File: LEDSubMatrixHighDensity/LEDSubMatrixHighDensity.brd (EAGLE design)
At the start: 16.9 x 135 mm, 129 parts, among them IC1 TLC5955DCAR, IC2 TLC5955DCAR, IC3 TLC5955DCAR, IC4 TLC5955DCAR, IC5 TLC5955DCAR, IC6 TLC5955DCAR, IC7 TLC5955DCAR, IC8 TLC5955DCAR

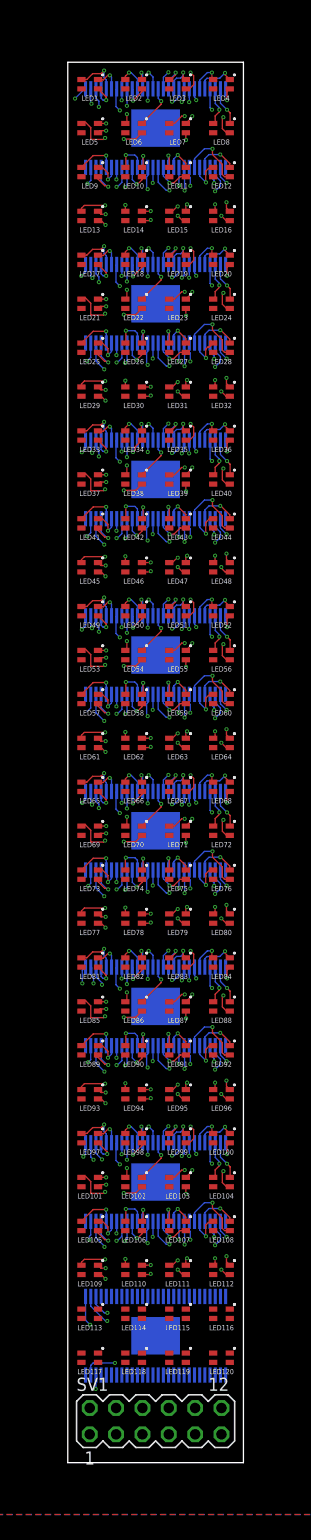
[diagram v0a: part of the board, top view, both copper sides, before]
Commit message: Finished routing traces on high density matrix PCB
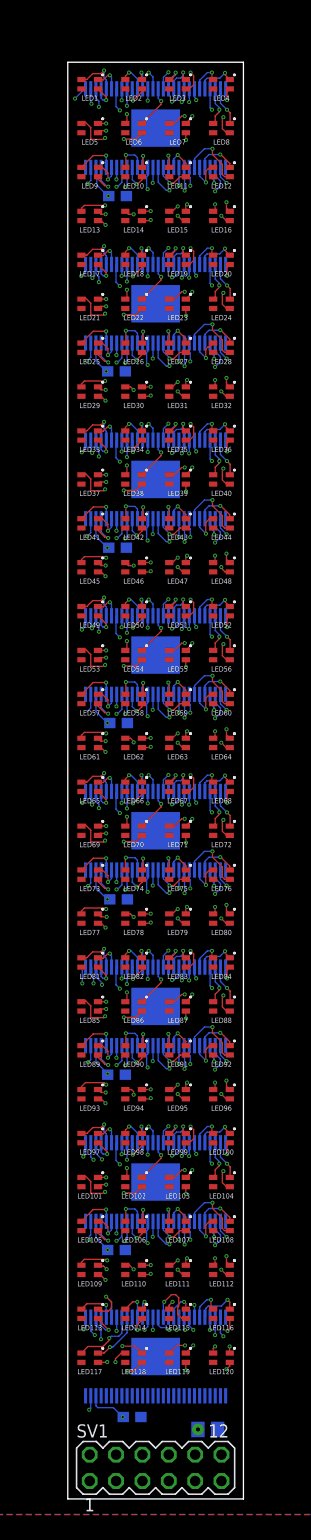
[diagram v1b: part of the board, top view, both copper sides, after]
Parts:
- added C1, C2, C3, C4, C5, C6, C7, C8: .1uF, rcl:C0603
- added C9: 10uF, rcl:C0805
- moved SV1 4.50 mm to (8.47, -135.5)
- moved IC8 2.00 mm to (8.47, -124.8)
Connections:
- net 3V3: now also C1.1, C2.1, C3.1, C4.1, C5.1, C6.1, C7.1, C8.1, C9.1
- net GND: now also C1.2, C2.2, C3.2, C4.2, C5.2, C6.2, C7.2, C8.2, C9.2
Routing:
- net N$LEDG118_IC8_PIN15: track 0.00 -> 11.0 mm, vias 0 -> 2
- net N$LEDR118_IC8_PIN14: track 0.00 -> 9.08 mm, vias 0 -> 2
- net 3V3: track 18.4 -> 26.6 mm, vias 7 -> 9
- net N$LEDB118_IC8_PIN13: track 0.00 -> 7.77 mm, vias 0 -> 2
- net N$LEDB120_IC8_PIN25: track 0.00 -> 7.18 mm, vias 0 -> 2
- net N$LEDB116_IC8_PIN22: track 0.00 -> 6.71 mm, vias 0 -> 2
- net N$LEDB119_IC8_PIN19: track 0.00 -> 6.59 mm, vias 0 -> 2
- net N$LEDR117_IC8_PIN8: track 0.00 -> 6.35 mm, vias 0 -> 1
- net N$LEDB115_IC8_PIN16: track 0.00 -> 5.92 mm, vias 0 -> 1
- net N$LEDB117_IC8_PIN7: track 0.00 -> 5.60 mm, vias 0 -> 2
- net N$LEDG117_IC8_PIN9: track 0.00 -> 5.11 mm, vias 0 -> 1
- net N$LEDG113_IC8_PIN6: track 0.00 -> 5.01 mm, vias 0 -> 1
- net LAT: track 144.8 -> 149.7 mm
- net SIN_5,6: track 63.0 -> 67.7 mm
- net N$LEDR119_IC8_PIN20: track 0.00 -> 4.58 mm, vias 0 -> 2
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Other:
- board size 16.9 x 135 mm -> 16.9 x 138.5 mm

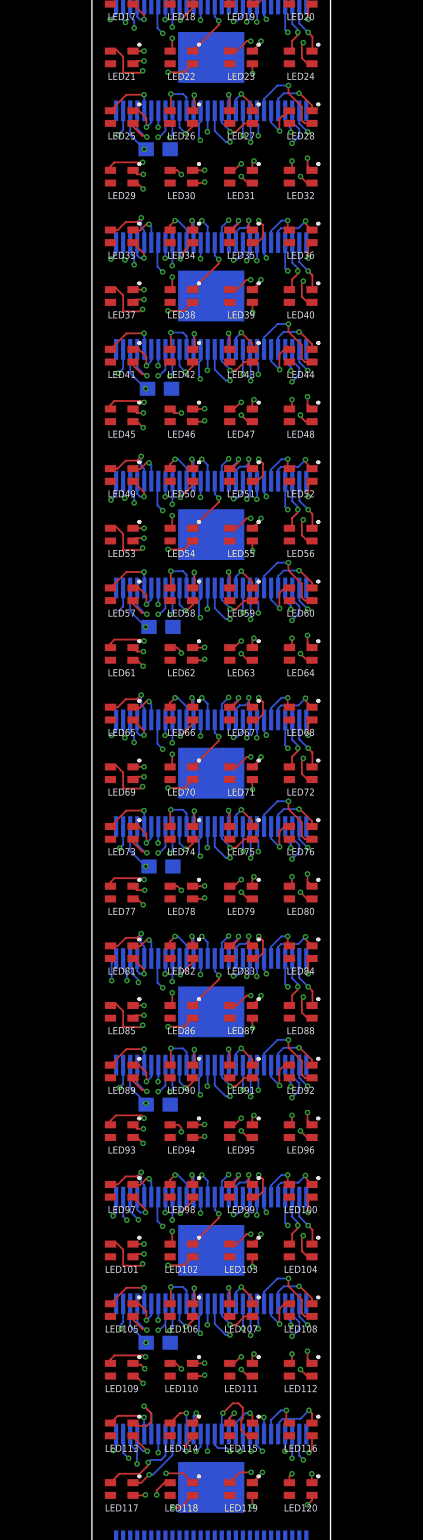
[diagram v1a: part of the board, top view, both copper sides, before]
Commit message: High density PCB fixes
Fixed airwires errors and grouped components on schematic
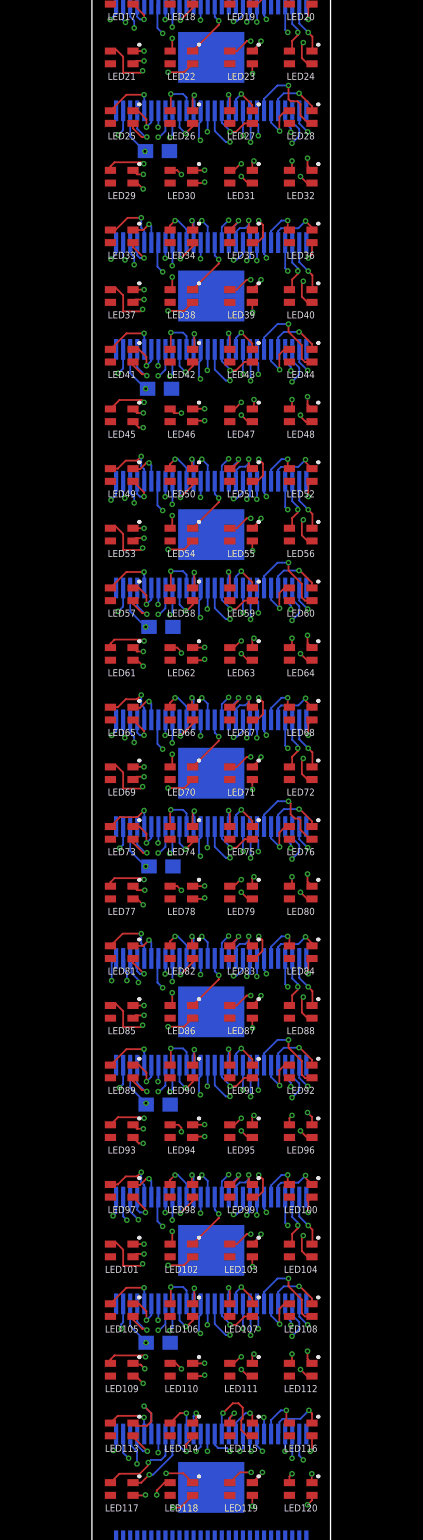
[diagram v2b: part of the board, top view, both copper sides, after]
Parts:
- moved C2 0.14 mm to (4.65, -29.9)
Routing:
- net GSCLK: vias 7 -> 8

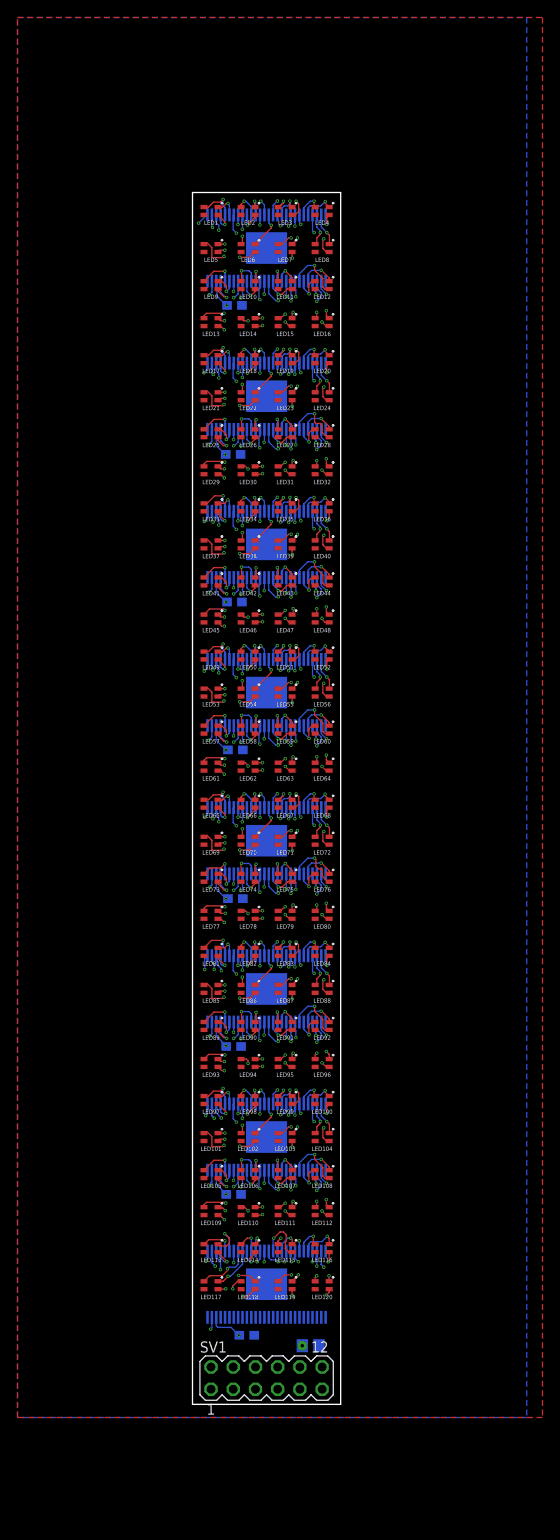
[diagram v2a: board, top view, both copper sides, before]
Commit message: Finalized LED Matrix schematic and board files
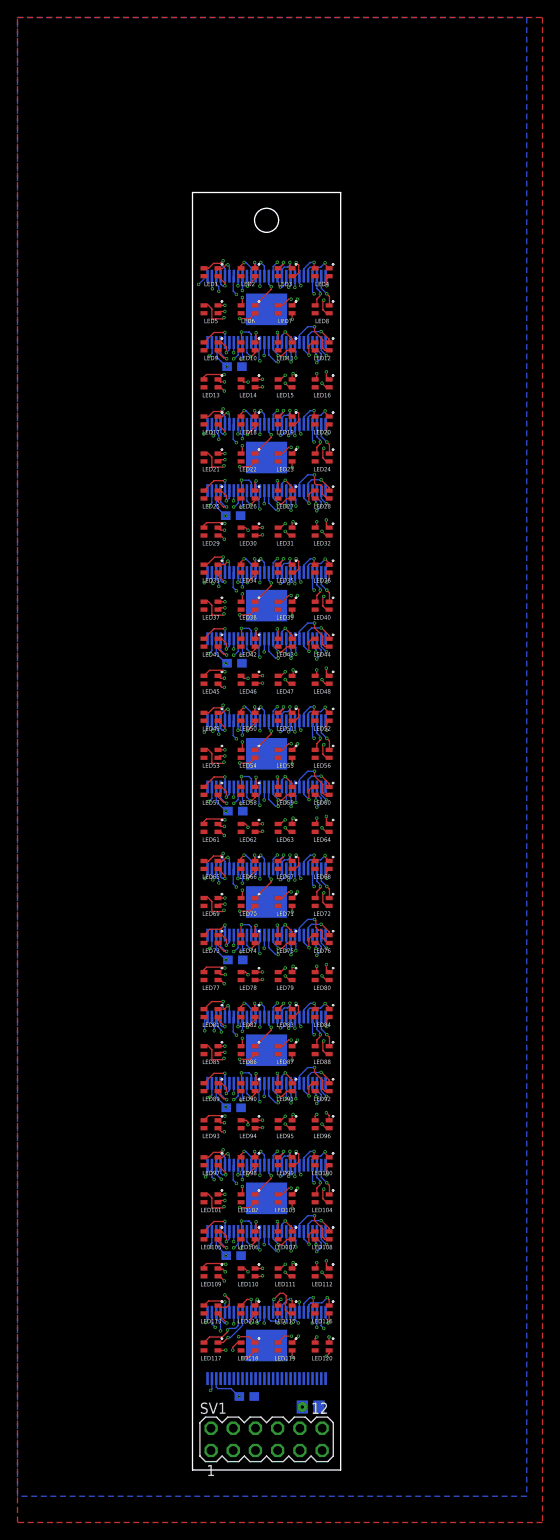
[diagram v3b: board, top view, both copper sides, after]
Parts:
- moved IC8 7.00 mm to (8.47, -131.8)
- moved IC4 7.00 mm to (8.47, -64.2)
- moved LED53 7.00 mm to (2.12, -64.2)
- moved LED54 7.00 mm to (6.35, -64.2)
- moved LED55 7.00 mm to (10.6, -64.2)
- moved LED56 7.00 mm to (14.8, -64.2)
- moved LED57 7.00 mm to (2.12, -68.4)
- moved LED58 7.00 mm to (6.35, -68.4)
- moved LED59 7.00 mm to (10.6, -68.4)
- moved LED60 7.00 mm to (14.8, -68.4)
- moved C2 7.00 mm to (4.65, -36.9)
- moved C3 7.00 mm to (4.80, -53.8)
- moved C4 7.00 mm to (4.90, -70.7)
- moved C5 7.00 mm to (4.90, -87.7)
- moved C6 7.00 mm to (4.70, -104.6)
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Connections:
- net 142142 renamed N$1
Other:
- board size 16.9 x 138.5 mm -> 16.9 x 146 mm
